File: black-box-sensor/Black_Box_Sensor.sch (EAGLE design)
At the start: 4 parts, among them U1 ADXL375, U2 ADXL375, U3 ATMEGA32U4-AU, U4 FXAS21002CQR1

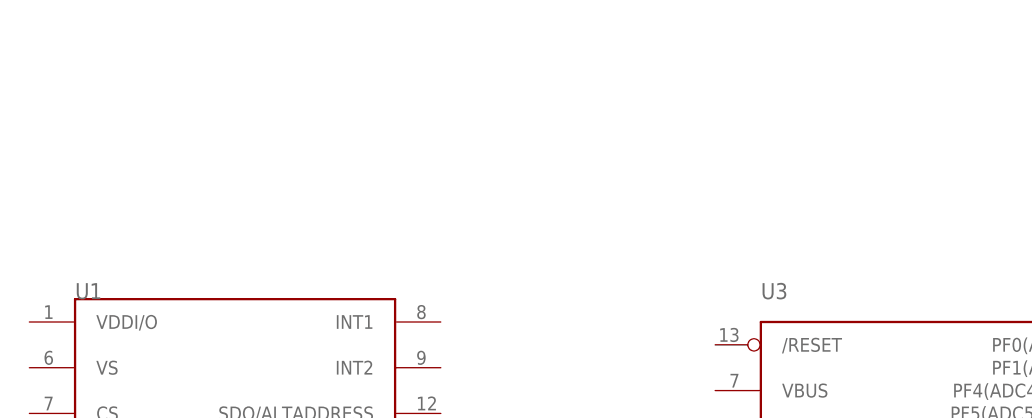
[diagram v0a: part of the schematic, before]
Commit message: voltage regulator addition
added voltage reg to the library, and added appropriate parts to the schematic for the voltage regulator to work
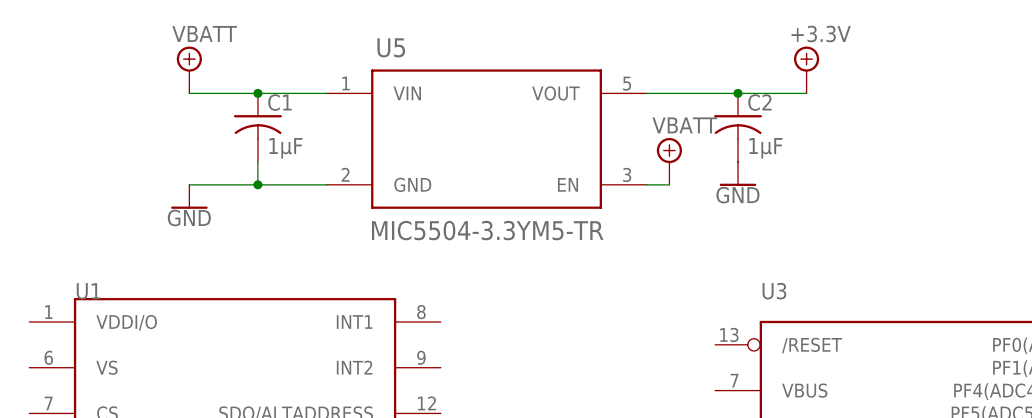
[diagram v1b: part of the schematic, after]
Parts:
- added C1, C2: 1µF, rcl:C-USC0603
- added U5: MIC5504-3.3YM5-TR, BBS_Library:MIC5504-3.3YM5-TR
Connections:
- new net +3.3V: C2.1, U5.VOUT
- new net GND: C1.2, C2.2, U5.GND
- new net VBATT: C1.1, U5.EN, U5.VIN
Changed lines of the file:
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@@
 <?xml version="1.0" encoding="utf-8"?>
 <!DOCTYPE eagle SYSTEM "eagle.dtd">
-<eagle version="9.6.2">
+<eagle version="9.5.1">
 <drawing>
 <settings>
@@
 <layers>
 <layer number="1" name="Top" color="4" fill="1" visible="no" active="no"/>
+<layer number="2" name="Route2" color="16" fill="1" visible="no" active="no"/>
+<layer number="3" name="Route3" color="17" fill="1" visible="no" active="no"/>
+<layer number="4" name="Route4" color="18" fill="1" visible="no" active="no"/>
+<layer number="5" name="Route5" color="19" fill="1" visible="no" active="no"/>
+<layer number="6" name="Route6" color="25" fill="1" visible="no" active="no"/>
+<layer number="7" name="Route7" color="26" fill="1" visible="no" active="no"/>
+<layer number="8" name="Route8" color="27" fill="1" visible="no" active="no"/>
+<layer number="9" name="Route9" color="28" fill="1" visible="no" active="no"/>
+<layer number="10" name="Route10" color="29" fill="1" visible="no" active="no"/>
+<layer number="11" name="Route11" color="30" fill="1" visible="no" active="no"/>
+<layer number="12" name="Route12" color="20" fill="1" visible="no" active="no"/>
+<layer number="13" name="Route13" color="21" fill="1" visible="no" active="no"/>
+<layer number="14" name="Route14" color="22" fill="1" visible="no" active="no"/>
+<layer number="15" name="Route15" color="23" fill="1" visible="no" active="no"/>
 <layer number="16" name="Bottom" color="1" fill="1" visible="no" active="no"/>
 <layer number="17" name="Pads" color="2" fill="1" visible="no" active="no"/>
@@
 <part name="U3" library="BBS_Library" deviceset="ATMEGA32U4" device="-AU"/>
 <part name="U4" library="BBS_Library" deviceset="FXAS21002CQR1" device=""/>
+<part name="U5" library="BBS_Library" deviceset="MIC5504-3.3YM5-TR" device=""/>
+<part name="SUPPLY1" library="RoboJackets-Supplies" deviceset="VBATT" device=""/>
+<part name="GND1" library="SparkFun-PowerSymbols" library_urn="urn:adsk.eagle:library:530" deviceset="GND" device=""/>
+<part name="C1" library="rcl" library_urn="urn:adsk.eagle:library:334" deviceset="C-US" device="C0603" package3d_urn="urn:adsk.eagle:package:23616/2" value="1µF">
+<spice>
+<pinmapping spiceprefix="C">
+<pinmap gate="G$1" pin="1" pinorder="1"/>
+<pinmap gate="G$1" pin="2" pinorder="2"/>
+</pinmapping>
+</spice>
+<attribute name="DKPN" value="CC0603KRX7R6BB105"/>
+<attribute name="VOLTAGE" value="10V"/>
+</part>
+<part name="C2" library="rcl" library_urn="urn:adsk.eagle:library:334" deviceset="C-US" device="C0603" package3d_urn="urn:adsk.eagle:package:23616/2" value="1µF">
+<spice>
+<pinmapping spiceprefix="C">
+<pinmap gate="G$1" pin="1" pinorder="1"/>
+<pinmap gate="G$1" pin="2" pinorder="2"/>
+</pinmapping>
+</spice>
+<attribute name="DKPN" value="CC0603KRX7R6BB105"/>
+<attribute name="VOLTAGE" value="10V"/>
+</part>
+<part name="GND2" library="SparkFun-PowerSymbols" library_urn="urn:adsk.eagle:library:530" deviceset="GND" device=""/>
+<part name="SUPPLY2" library="RoboJackets-Supplies" deviceset="VBATT" device=""/>
+<part name="SUPPLY3" library="RoboJackets-Supplies" deviceset="+3.3V" device=""/>
 </parts>
 <sheets>
@@
 <attribute name="VALUE" x="27.94" y="-4.318" size="1.778" layer="96" align="top-left"/>
 </instance>
+<instance part="U5" gate="A" x="76.2" y="111.76" smashed="yes">
+<attribute name="NAME" x="63.8556" y="120.8786" size="2.0828" layer="95" ratio="6" rot="SR0"/>
+<attribute name="VALUE" x="63.2206" y="100.5586" size="2.0828" layer="96" ratio="6" rot="SR0"/>
+</instance>
+<instance part="SUPPLY1" gate="G$1" x="43.18" y="119.38" smashed="yes">
+<attribute name="VALUE" x="41.275" y="122.555" size="1.778" layer="96"/>
+</instance>
+<instance part="GND1" gate="1" x="43.18" y="104.14" smashed="yes">
+<attribute name="VALUE" x="43.18" y="103.886" size="1.778" layer="96" align="top-center"/>
+</instance>
+<instance part="C1" gate="G$1" x="50.8" y="114.3" smashed="yes">
+<attribute name="NAME" x="51.816" y="114.935" size="1.778" layer="95"/>
+<attribute name="VALUE" x="51.816" y="110.109" size="1.778" layer="96"/>
+<attribute name="VOLTAGE" x="50.8" y="114.3" size="1.778" layer="96" display="off"/>
+<attribute name="DKPN" x="50.8" y="114.3" size="1.778" layer="96" display="off"/>
+</instance>
+<instance part="C2" gate="G$1" x="104.14" y="114.3" smashed="yes">
+<attribute name="NAME" x="105.156" y="114.935" size="1.778" layer="95"/>
+<attribute name="VALUE" x="105.156" y="110.109" size="1.778" layer="96"/>
+<attribute name="VOLTAGE" x="104.14" y="114.3" size="1.778" layer="96" display="off"/>
+<attribute name="DKPN" x="104.14" y="114.3" size="1.778" layer="96" display="off"/>
+</instance>
+<instance part="GND2" gate="1" x="104.14" y="106.68" smashed="yes">
+<attribute name="VALUE" x="104.14" y="106.426" size="1.778" layer="96" align="top-center"/>
+</instance>
+<instance part="SUPPLY2" gate="G$1" x="96.52" y="109.22" smashed="yes">
+<attribute name="VALUE" x="94.615" y="112.395" size="1.778" layer="96"/>
+</instance>
+<instance part="SUPPLY3" gate="P" x="111.76" y="119.38" smashed="yes">
+<attribute name="VALUE" x="109.855" y="122.555" size="1.778" layer="96"/>
+</instance>
 </instances>
 <busses>
 </busses>
 <nets>
+<net name="VBATT" class="0">
+<segment>
+<pinref part="SUPPLY1" gate="G$1" pin="VBATT"/>
+<pinref part="U5" gate="A" pin="VIN"/>
+<wire x1="43.18" y1="116.84" x2="50.8" y2="116.84" width="0.1524" layer="91"/>
+<pinref part="C1" gate="G$1" pin="1"/>
+<wire x1="50.8" y1="116.84" x2="58.42" y2="116.84" width="0.1524" layer="91"/>
+<junction x="50.8" y="116.84"/>
+</segment>
+<segment>
+<pinref part="SUPPLY2" gate="G$1" pin="VBATT"/>
+<pinref part="U5" gate="A" pin="EN"/>
+<wire x1="96.52" y1="106.68" x2="93.98" y2="106.68" width="0.1524" layer="91"/>
+</segment>
+</net>
+<net name="GND" class="0">
+<segment>
+<pinref part="GND1" gate="1" pin="GND"/>
+<pinref part="U5" gate="A" pin="GND"/>
+<wire x1="43.18" y1="106.68" x2="50.8" y2="106.68" width="0.1524" layer="91"/>
+<pinref part="C1" gate="G$1" pin="2"/>
+<wire x1="50.8" y1="106.68" x2="58.42" y2="106.68" width="0.1524" layer="91"/>
+<wire x1="50.8" y1="109.22" x2="50.8" y2="106.68" width="0.1524" layer="91"/>
+<junction x="50.8" y="106.68"/>
+</segment>
+<segment>
+<pinref part="GND2" gate="1" pin="GND"/>
+<pinref part="C2" gate="G$1" pin="2"/>
+</segment>
+</net>
+<net name="+3.3V" class="0">
+<segment>
+<pinref part="U5" gate="A" pin="VOUT"/>
+<pinref part="C2" gate="G$1" pin="1"/>
+<wire x1="93.98" y1="116.84" x2="104.14" y2="116.84" width="0.1524" layer="91"/>
+<wire x1="104.14" y1="116.84" x2="111.76" y2="116.84" width="0.1524" layer="91"/>
+<junction x="104.14" y="116.84"/>
+<pinref part="SUPPLY3" gate="P" pin="+3.3V"/>
+</segment>
+</net>
 </nets>
 </sheet>
@@
 </schematic>
 </drawing>
+<compatibility>
+<note version="8.2" severity="warning">
+Since Version 8.2, EAGLE supports online libraries. The ids
+of those online libraries will not be understood (or retained)
+with this version.
+</note>
+<note version="8.3" severity="warning">
+Since Version 8.3, EAGLE supports URNs for individual library
+assets (packages, symbols, and devices). The URNs of those assets
+will not be understood (or retained) with this version.
+</note>
+<note version="8.3" severity="warning">
+Since Version 8.3, EAGLE supports the association of 3D packages
+with devices in libraries, schematics, and board files. Those 3D
+packages will not be understood (or retained) with this version.
+</note>
+<note version="8.4" severity="warning">
+Since Version 8.4, EAGLE supports properties for SPICE simulation.
+Probes in schematics and SPICE mapping objects found in parts and library devices
+will not be understood with this version. Update EAGLE to the latest version
+for full support of SPICE simulation.
+</note>
+</compatibility>
 </eagle>

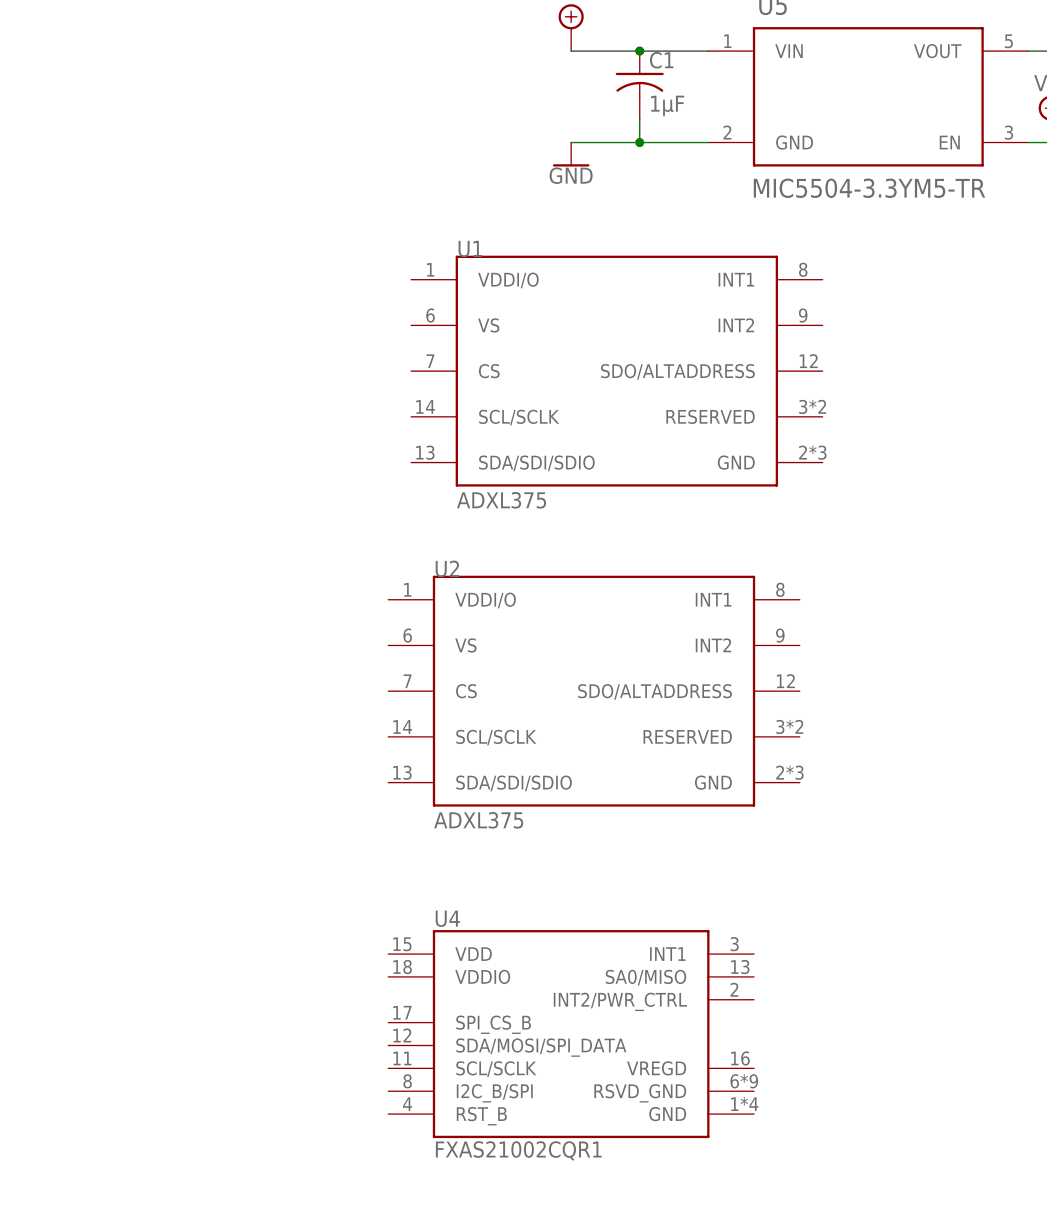
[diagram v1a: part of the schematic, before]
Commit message: start schematic for accelerometer and gyro
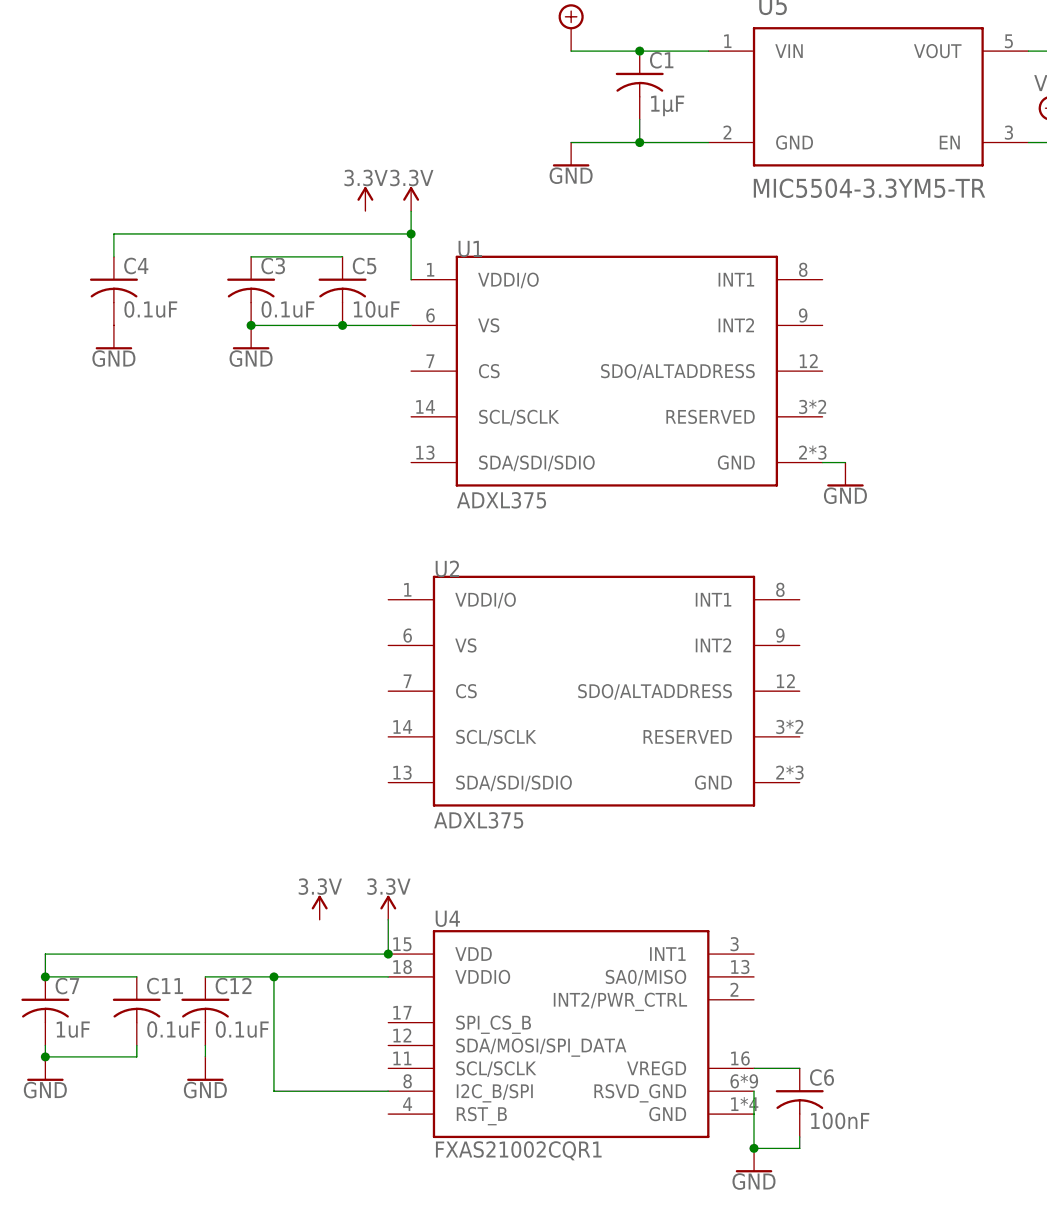
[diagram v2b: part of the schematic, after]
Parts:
- added C11, C12: 0.1uF, rcl:C-USC0603K
- added C3, C4: 0.1uF, rcl:C-USC0603
- added C5: 10uF, rcl:C-USC0603
- added C6: 100nF, rcl:C-USC0603
- added C7: 1uF, rcl:C-USC0603K
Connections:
- new net 3.3V: C11.1, C4.1, C7.1, U1.VDDI/O, U4.VDD
- new net N$1: C6.1, U4.VREGD
- new net N$2: C3.1, C5.1
- new net N$3: C12.1, U4.I2C_B/SPI, U4.VDDIO
- net GND: now also C11.2, C12.2, C3.2, C4.2, C5.2, C6.2, C7.2, U1.GND, U1.VS, U4.GND, U4.RSVD_GND

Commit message: quick meeting edits
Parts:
- removed C5: 10uF, rcl:C-USC0603
- removed C7: 1uF, rcl:C-USC0603K
- added U6: NL27WZ32USG, Hocki_Library:NL27WZ32USG
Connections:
- removed net N$2: C3.1, C5.1
- removed net N$3: C12.1, U4.I2C_B/SPI, U4.VDDIO
- net 3.3V: now also C12.1, C3.1, U4.I2C_B/SPI, U4.RST_B, U4.VDDIO; no longer C7.1
- net GND: no longer C5.2, C7.2
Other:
- moved on the sheet: C11, C12, C4, C6, U3, U4
